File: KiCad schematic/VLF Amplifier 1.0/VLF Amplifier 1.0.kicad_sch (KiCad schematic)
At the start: 25 parts, among them J1 To radio reciever (50 Ohm), Q1 2SK241, Q2 BC547

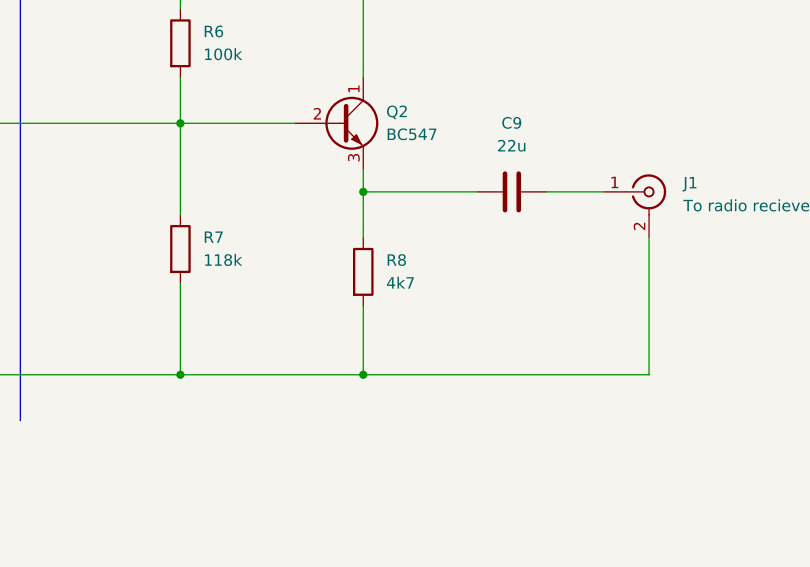
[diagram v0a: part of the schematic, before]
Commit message: R8 4k7 -> 1k to increase the current. Gives amplification 2x more.
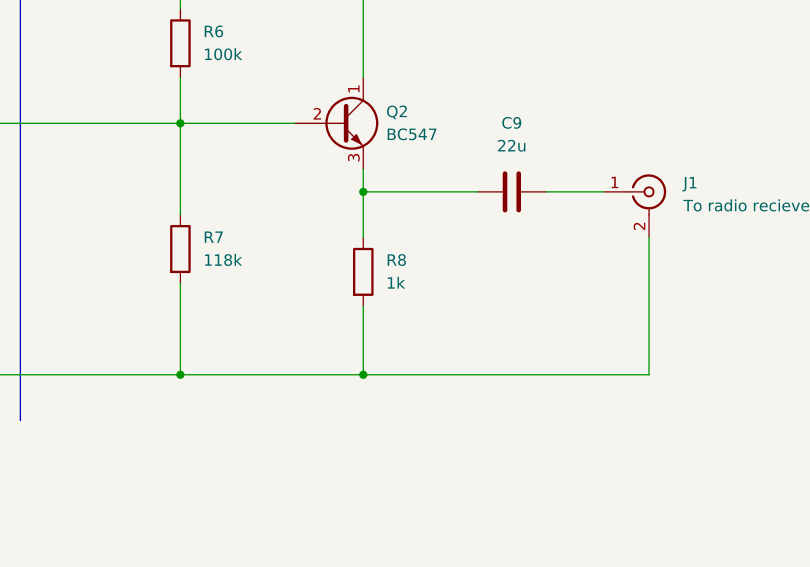
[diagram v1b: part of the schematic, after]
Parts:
- R8: value 4k7 -> 1k
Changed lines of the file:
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@@
   (title_block
     (title "VLF amplifier")
-    (date "2023-01-02")
-    (rev "1")
+    (date "2023-01-07")
+    (rev "2")
     (comment 1 "Nicklas Norling, SA5NNN, original from https://www.prinz.nl/SAQ.html")
     (comment 2 "VLF amplifier for ferrite antenna to 50 ohm reciever.")
@@
       (effects (font (size 1.27 1.27)) (justify left))
     )
-    (property "Value" "4k7" (id 1) (at 222.25 71.1199 0)
+    (property "Value" "1k" (id 1) (at 222.25 71.1199 0)
       (effects (font (size 1.27 1.27)) (justify left))
     )
@@
     )
     (path "/35363222-2616-4cf7-b3ad-0f5ee85dbf49"
-      (reference "R8") (unit 1) (value "4k7") (footprint "")
+      (reference "R8") (unit 1) (value "1k") (footprint "")
     )
     (path "/87f239f3-12ef-47dd-977e-9faee08e138a"
